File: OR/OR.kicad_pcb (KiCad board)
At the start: 2 copper layers, 20 x 22.5 mm, 9 parts, among them J1 AudioJack2_SwitchT, J2 AudioJack2_SwitchT, J3 AudioJack2_SwitchT, Q1 BSS84, Q2 BSS84, Q3 BSS84, Q4 BSS84, Q5 BSS84

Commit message: Add OR gate front panel
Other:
- board text added: "Passive OR"
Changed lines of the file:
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@@
 		)
 		(property "Value" "AudioJack2_SwitchT"
-			(at 22.75 -8.25 -0)
+			(at 22.75 -8.25 0)
 			(layer "B.Fab")
 			(effects
@@
 		(tags "SOT TO_SOT_SMD")
 		(property "Reference" "Q2"
-			(at -1 -2.5 360)
+			(at -1 -2.5 0)
 			(layer "B.SilkS")
 			(effects
@@
 		)
 		(property "Value" "BSS84"
-			(at 0 -2.4 360)
+			(at 0 -2.4 0)
 			(layer "B.Fab")
 			(effects
@@
 		)
 		(fp_text user "${REFERENCE}"
-			(at 0 0 360)
+			(at 0 0 0)
 			(layer "B.Fab")
 			(effects
@@
 		(tags "SOT TO_SOT_SMD")
 		(property "Reference" "Q5"
-			(at 0.6875 -2.5 360)
+			(at 0.6875 -2.5 0)
 			(layer "B.SilkS")
 			(effects
@@
 		)
 		(property "Value" "BSS84"
-			(at 0 -2.4 360)
+			(at 0 -2.4 0)
 			(layer "B.Fab")
 			(effects
@@
 		)
 		(fp_text user "${REFERENCE}"
-			(at 0 0 360)
+			(at 0 0 0)
 			(layer "B.Fab")
 			(effects
@@
 		(layer "Edge.Cuts")
 	)
+	(gr_text "Passive\nOR"
+		(at 141.2 79.45 0)
+		(layer "B.SilkS")
+		(effects
+			(font
+				(size 1 1)
+				(thickness 0.15)
+			)
+			(justify bottom mirror)
+		)
+	)
 	(via

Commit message: Finalize modules
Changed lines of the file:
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@@
 			(plot_on_all_layers_selection 0x0000000_00000000)
 			(disableapertmacros no)
-			(usegerberextensions no)
-			(usegerberattributes yes)
-			(usegerberadvancedattributes yes)
-			(creategerberjobfile yes)
+			(usegerberextensions yes)
+			(usegerberattributes no)
+			(usegerberadvancedattributes no)
+			(creategerberjobfile no)
 			(dashed_line_dash_ratio 12.000000)
 			(dashed_line_gap_ratio 3.000000)
@@
 			(psa4output no)
 			(plotreference yes)
-			(plotvalue yes)
+			(plotvalue no)
 			(plotfptext yes)
 			(plotinvisibletext no)
 			(sketchpadsonfab no)
-			(subtractmaskfromsilk no)
+			(subtractmaskfromsilk yes)
 			(outputformat 1)
 			(mirror no)
-			(drillshape 1)
+			(drillshape 0)
 			(scaleselection 1)
-			(outputdirectory "")
+			(outputdirectory "out/")
 		)
 	)
@@
 		(at 131.25 93 90)
 		(property "Reference" "J2"
-			(at 0 -6.75 90)
+			(at 5.5 -4.25 180)
 			(layer "F.SilkS")
 			(effects
@@
 		(at 131.25 79.5 90)
 		(property "Reference" "J1"
-			(at 0 -6.75 90)
-			(layer "F.SilkS")
-			(effects
+			(at -5.5 -4.25 180)
+			(layer "F.SilkS")
+			(effects

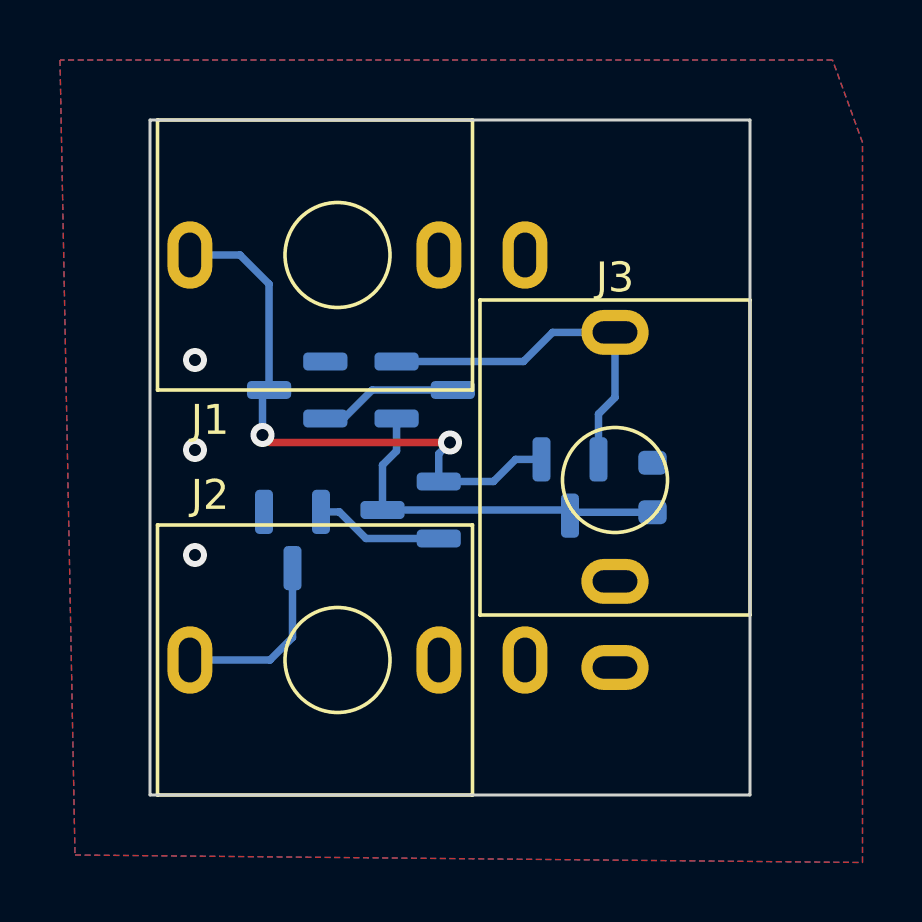
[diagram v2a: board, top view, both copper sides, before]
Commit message: Add pulldown when OR inputs are low
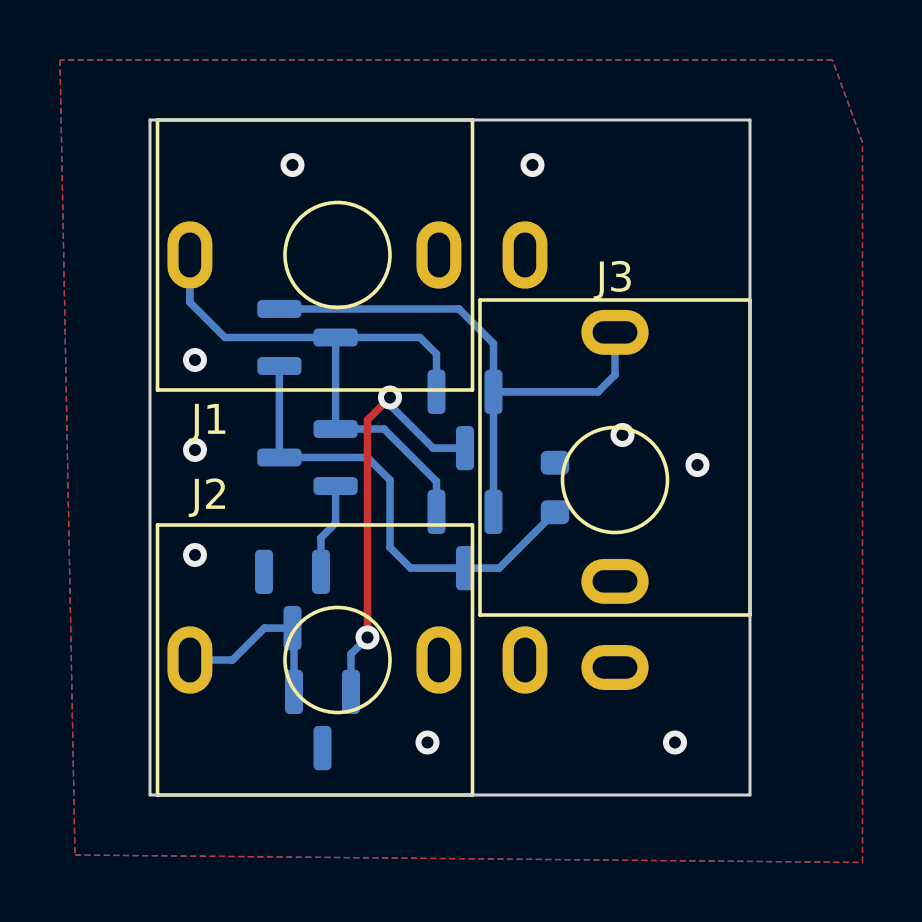
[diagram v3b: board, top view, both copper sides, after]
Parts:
- removed the Q1 at (129.9, 84.0)
- added Q5: BSS84, Package_TO_SOT_SMD:SOT-23, B.Cu at (135.5, 85.0)
- added Q6: BSS84, Package_TO_SOT_SMD:SOT-23, B.Cu at (130.8, 95.0)
- moved Q3 4.28 mm to (130.2, 82.2)
- moved Q4 3.91 mm to (135.5, 89.0)
- moved Q2 3.86 mm to (130.2, 86.2)
- moved R1 3.25 mm to (138.5, 87.2)
- moved Q1 2.00 mm to (129.8, 91.0)
- renumbered Q3 to Q1, Q5 to Q2, Q2 to Q3
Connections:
- J1 pad T: Net-(Q1-D) (its old number) -> Net-(Q2-G)
- Q2 pad 1: Net-(Q1-D) (its old number) -> Net-(Q2-G)
- Q3 pad 3: Net-(Q1-S) (its old number) -> Net-(Q2-G)
- Q4 pad 1: Net-(Q1-D) (its old number) -> Net-(Q2-G)
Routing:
- net Net-(Q2-G): track 0.00 -> 19.9 mm
- net Net-(Q1-D) (its old number): track 19.7 -> 0.00 mm, vias 2 -> 0
- net Net-(Q5-D): track 0.00 -> 13.7 mm, vias 0 -> 2
- net Net-(Q3-S): track 12.1 -> 18.9 mm
- net Net-(Q1-S) (its old number): track 4.64 -> 0.00 mm
- net Net-(Q2-D): track 12.4 -> 15.9 mm
- net Net-(Q1-S): track 4.29 -> 3.06 mm
- net GND: vias 3 -> 9
